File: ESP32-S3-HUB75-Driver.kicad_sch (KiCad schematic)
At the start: 21 parts, among them J1 Conn_02x08_Odd_Even, SW2 SW_SPST, SW3 SW_SPST, U1 ESP32-S3-WROOM-1-N16R2, U10 AP2112K-3.3, U2 74AHCT245PW,118, U3 74AHCT245PW,118

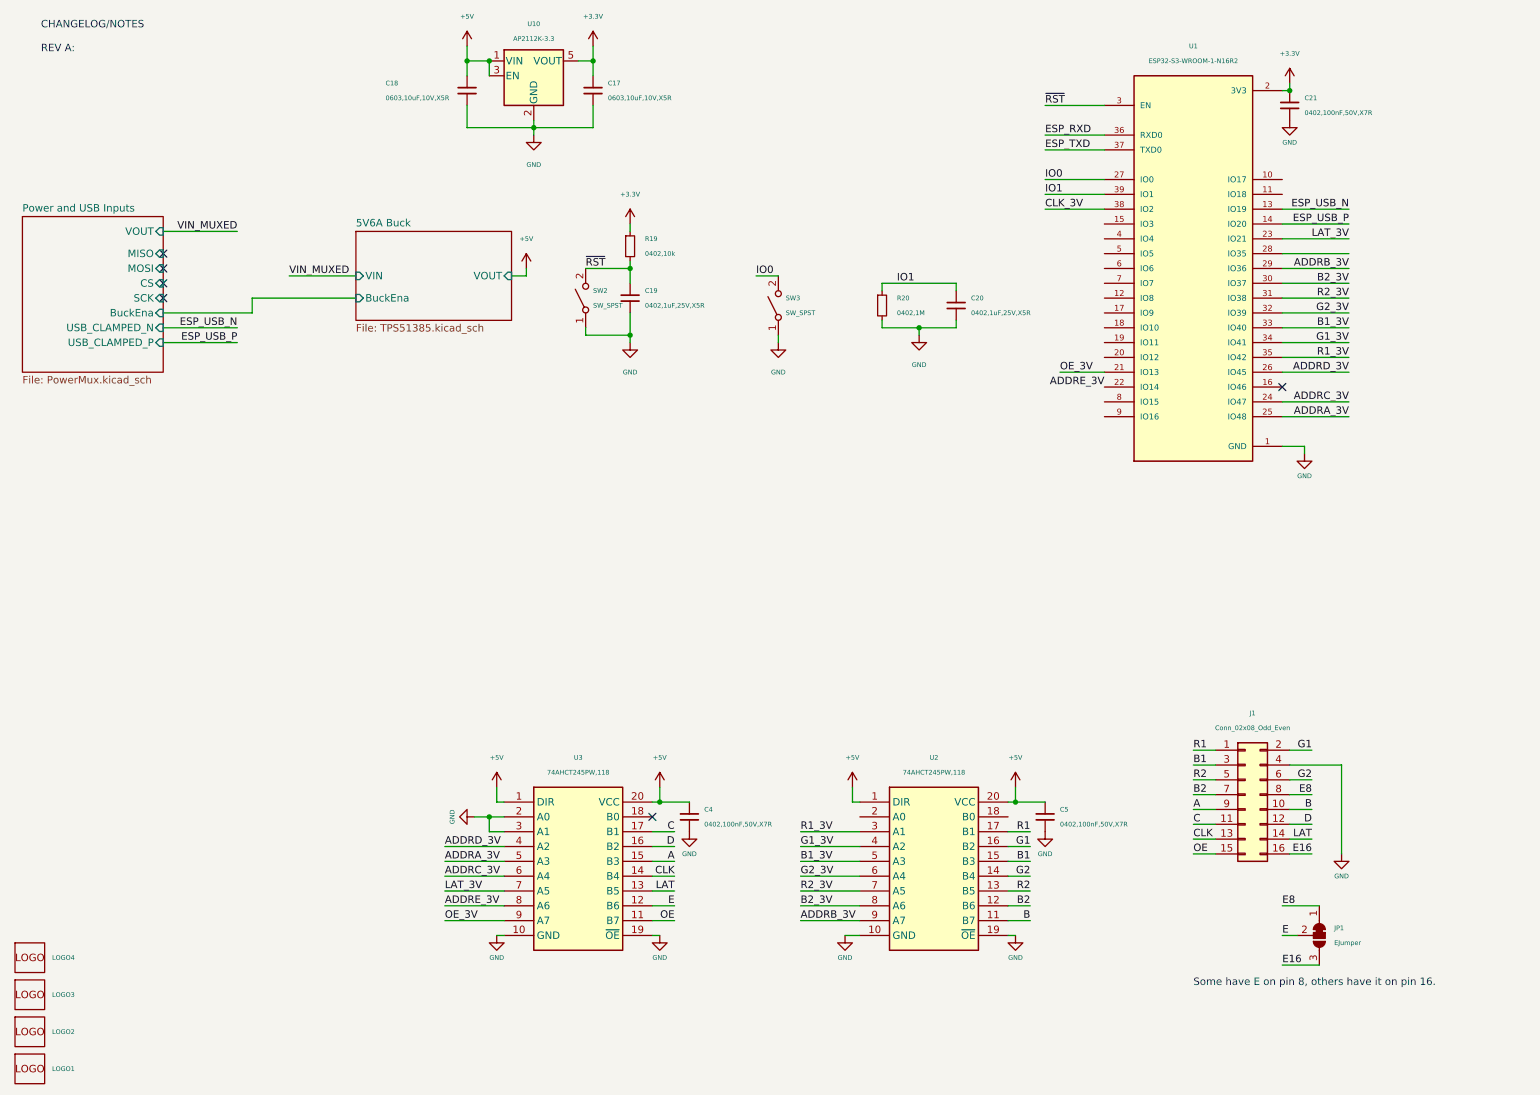
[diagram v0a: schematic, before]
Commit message: updated schematic to look neater
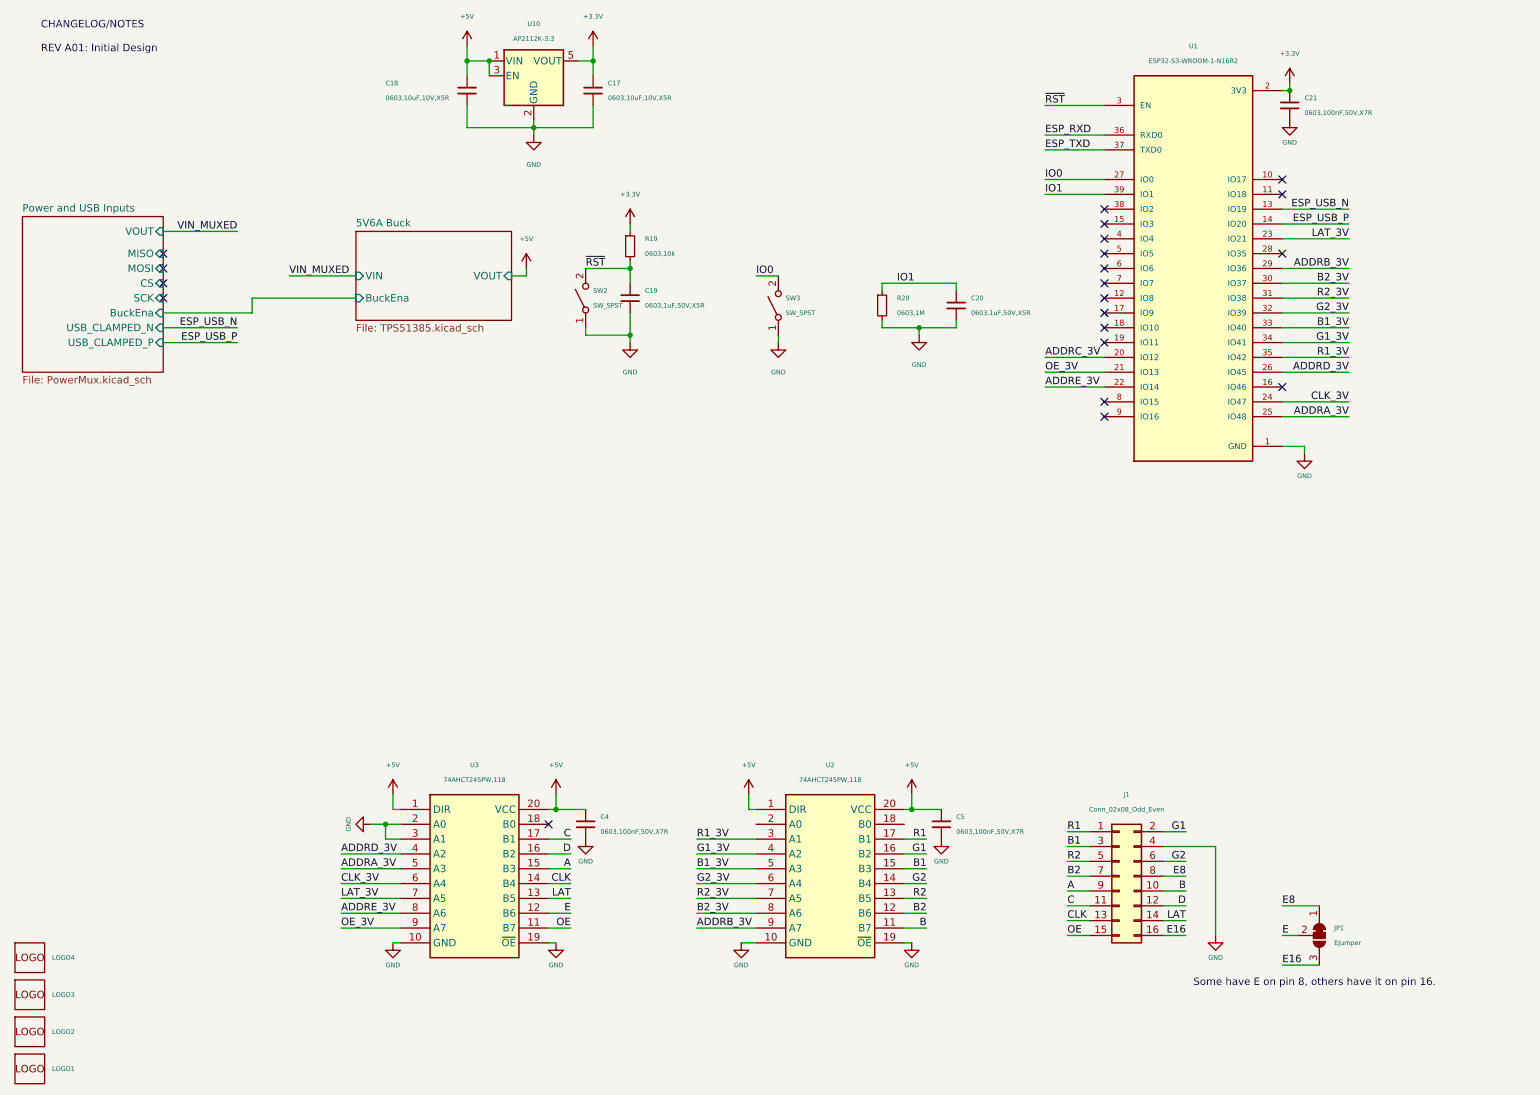
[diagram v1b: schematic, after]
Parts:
- C19, C20: value 0402,1uF,25V,X5R -> 0603,1uF,50V,X5R
- C21, C4, C5: value 0402,100nF,50V,X7R -> 0603,100nF,50V,X7R
- R19: value 0402,10k -> 0603,10k
- R20: value 0402,1M -> 0603,1M
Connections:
- net ADDRC_3V: now also U1.20 (IO12); no longer U1.24 (IO47), U3.6 (A4)
- net CLK_3V: now also U1.24 (IO47), U3.6 (A4); no longer U1.38 (IO2)
- no-connect marks 6 -> 21
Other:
- note added: "CHANGELOG/NOTES REV A01: Initial Design"
- note removed: "CHANGELOG/NOTES REV A:"
- moved on the sheet: C4, C5, J1, U2, U3
